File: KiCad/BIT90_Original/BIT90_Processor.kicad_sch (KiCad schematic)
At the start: 24 parts, among them SW65 RST, U1 D4016, U13 74LS138, U14 74LS05, U2 2764, U3 2764, U4 2764, U5 Z80, U6 74LS74, U8 74LS32

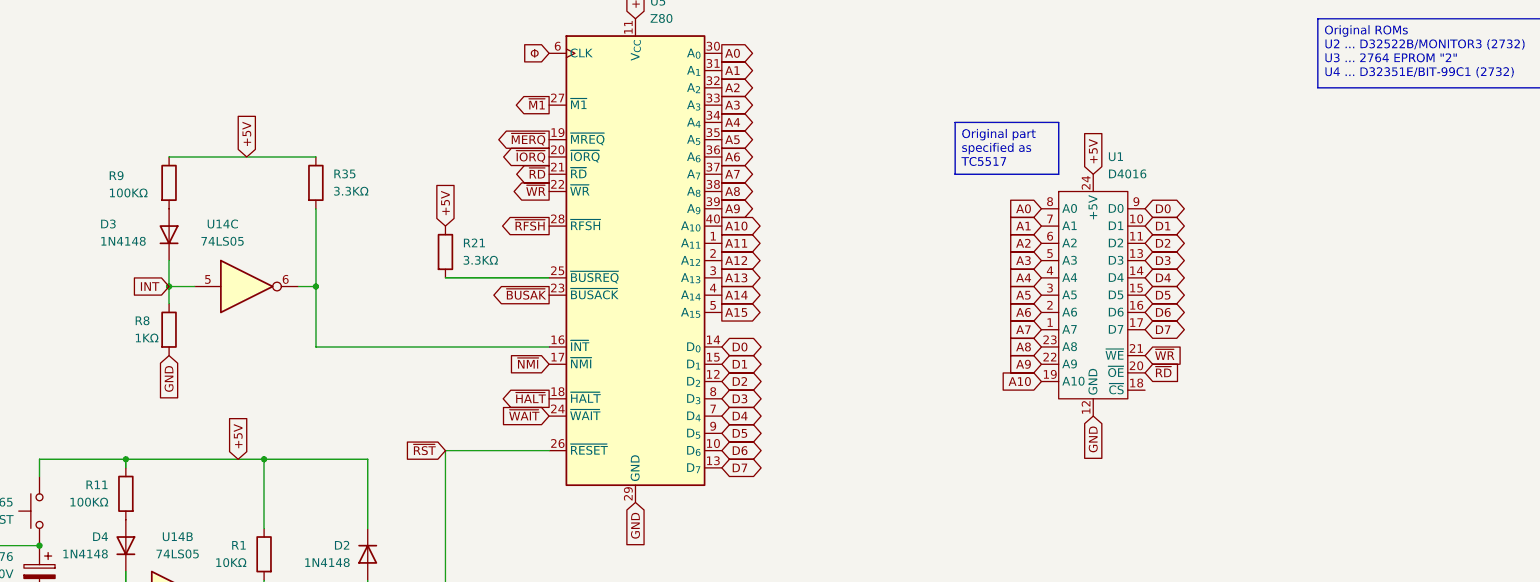
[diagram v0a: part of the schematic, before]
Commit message: Completed keyboard schematic
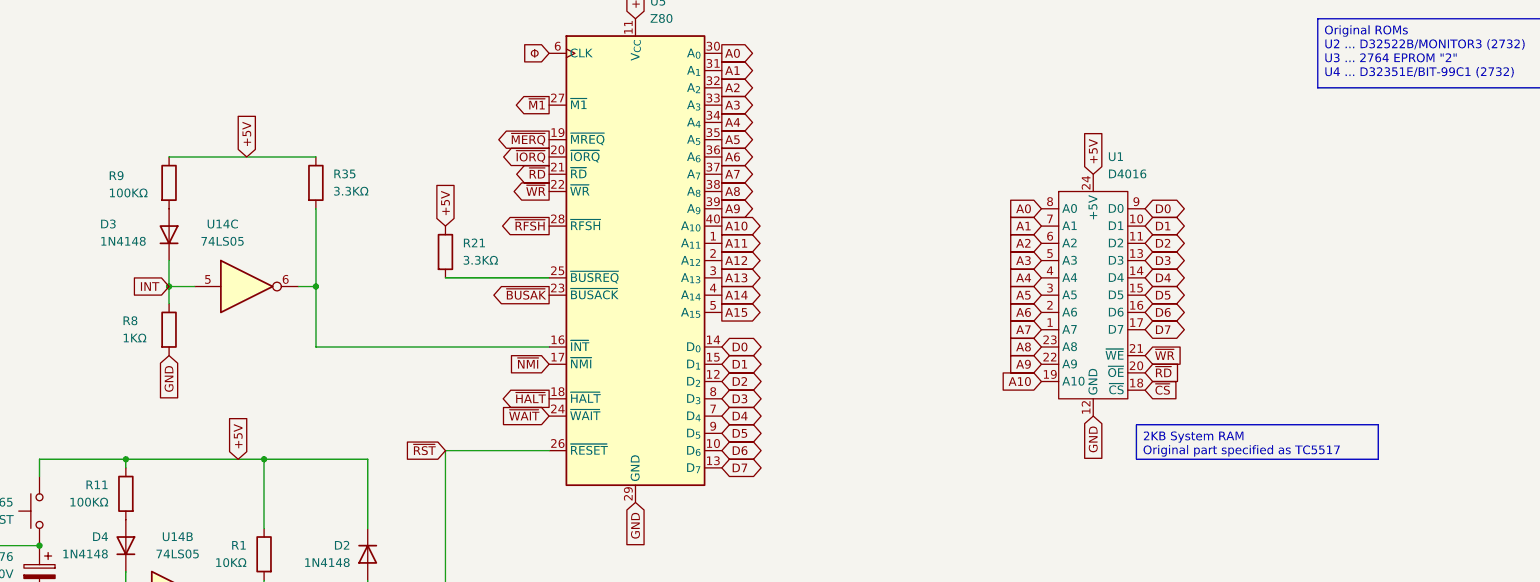
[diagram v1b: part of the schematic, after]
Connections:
- net ~{CS}: now also U1.18 (~{CS})
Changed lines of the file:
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@@
 		(comment 4 "Based on original schematics from BIT Corporation")
 	)
-	(text_box "Original part specified as TC5517"
+	(text_box "2KB System RAM\nOriginal part specified as TC5517"
 		(exclude_from_sim no)
-		(at 176.53 105.41 0)
-		(size 15.24 7.62)
+		(at 203.2 149.86 0)
+		(size 35.56 5.08)
 		(margins 0.9525 0.9525 0.9525 0.9525)
 		(stroke
@@
 		)
 	)
+	(table
+		(column_count 2)
+		(border
+			(external yes)
+			(header yes)
+			(stroke
+				(width 0)
+				(type solid)
+			)
+		)
+		(separators
+			(rows yes)
+			(cols yes)
+			(stroke
+				(width 0)
+				(type solid)
+			)
+		)
+		(column_widths 20.32 20.32)
+		(row_heights 2.54 2.54 2.54 2.54)
+		(cells
+			(table_cell "~{MO}"
+				(exclude_from_sim no)
+				(at 72.39 72.39 0)
+				(size 20.32 2.54)
+				(margins 0.9525 0.9525 0.9525 0.9525)
+				(span 1 1)
+				(fill
+					(type none)
+				)
+				(effects
+					(font
+						(size 1.27 1.27)
+					)
+					(justify left top)
+				)
+			)
+			(table_cell "Monitor"
+				(exclude_from_sim no)
+				(at 92.71 72.39 0)
+				(size 20.32 2.54)
+				(margins 0.9525 0.9525 0.9525 0.9525)
+				(span 1 1)
+				(fill
+					(type none)
+				)
+				(effects
+					(font
+						(size 1.27 1.27)
+					)
+					(justify left top)
+				)
+			)
+			(table_cell "~{BA1} & ~{BA2}"
+				(exclude_from_sim no)
+				(at 72.39 74.93 0)
+				(size 20.32 2.54)
+				(margins 0.9525 0.9525 0.9525 0.9525)
+				(span 1 1)
+				(fill
+					(type none)
+				)
+				(effects
+					(font
+						(size 1.27 1.27)
+					)
+					(justify left top)
+				)
+			)
+			(table_cell "BASIC"
+				(exclude_from_sim no)
+				(at 92.71 74.93 0)
+				(size 20.32 2.54)
+				(margins 0.9525 0.9525 0.9525 0.9525)
+				(span 1 1)
+				(fill
+					(type none)
+				)
+				(effects
+					(font
+						(size 1.27 1.27)
+					)
+					(justify left top)
+				)
+			)
+			(table_cell "~{CS}"
+				(exclude_from_sim no)
+				(at 72.39 77.47 0)
+				(size 20.32 2.54)
+				(margins 0.9525 0.9525 0.9525 0.9525)
+				(span 1 1)
+				(fill
+					(type none)
+				)
+				(effects
+					(font
+						(size 1.27 1.27)
+					)
+					(justify left top)
+				)
+			)
+			(table_cell "System RAM"
+				(exclude_from_sim no)
+				(at 92.71 77.47 0)
+				(size 20.32 2.54)
+				(margins 0.9525 0.9525 0.9525 0.9525)
+				(span 1 1)
+				(fill
+					(type none)
+				)
+				(effects
+					(font
+						(size 1.27 1.27)
+					)
+					(justify left top)
+				)
+			)
+			(table_cell "~{CAR1} to ~{CAR4}"
+				(exclude_from_sim no)
+				(at 72.39 80.01 0)
+				(size 20.32 2.54)
+				(margins 0.9525 0.9525 0.9525 0.9525)
+				(span 1 1)
+				(fill
+					(type none)
+				)
+				(effects
+					(font
+						(size 1.27 1.27)
+					)
+					(justify left top)
+				)
+			)
+			(table_cell "Cartridge"
+				(exclude_from_sim no)
+				(at 92.71 80.01 0)
+				(size 20.32 2.54)
+				(margins 0.9525 0.9525 0.9525 0.9525)
+				(span 1 1)
+				(fill
+					(type none)
+				)
+				(effects
+					(font
+						(size 1.27 1.27)
+					)
+					(justify left top)
+				)
+			)
+		)
+	)
 	(global_label "D4"
 		(shape output)
@@
 		)
 	)
+	(global_label "~{CS}"
+		(shape input)
+		(at 204.47 144.78 0)
+		(fields_autoplaced yes)
+		(effects
+			(font
+				(size 1.27 1.27)
+			)
+			(justify left)
+		)
+		(property "Intersheetrefs" "${INTERSHEET_REFS}"
+			(at 209.9347 144.78 0)
+			(effects
+				(font
+					(size 1.27 1.27)
+				)
+				(justify left)
+				(hide yes)
+			)
+		)
+	)
 	(global_label "A11"
 		(shape input)
@@
 		(dnp no)
 		(property "Reference" "R8"
-			(at 55.88 134.62 0)
+			(at 54.102 134.62 0)
 			(effects
 				(font
@@
 		)
 		(property "Value" "1KΩ"
-			(at 55.88 137.16 0)
+			(at 54.102 137.16 0)
 			(effects
 				(font

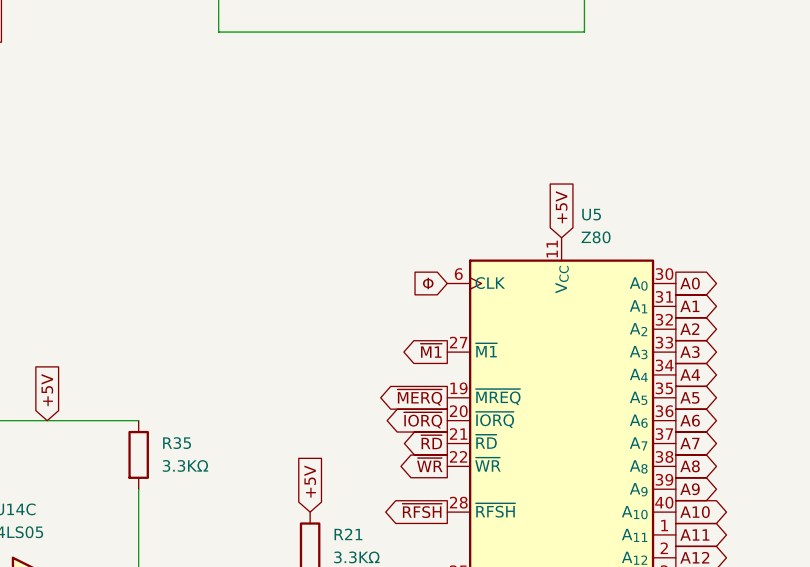
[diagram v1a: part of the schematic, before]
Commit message: Added "Video Control" schematic
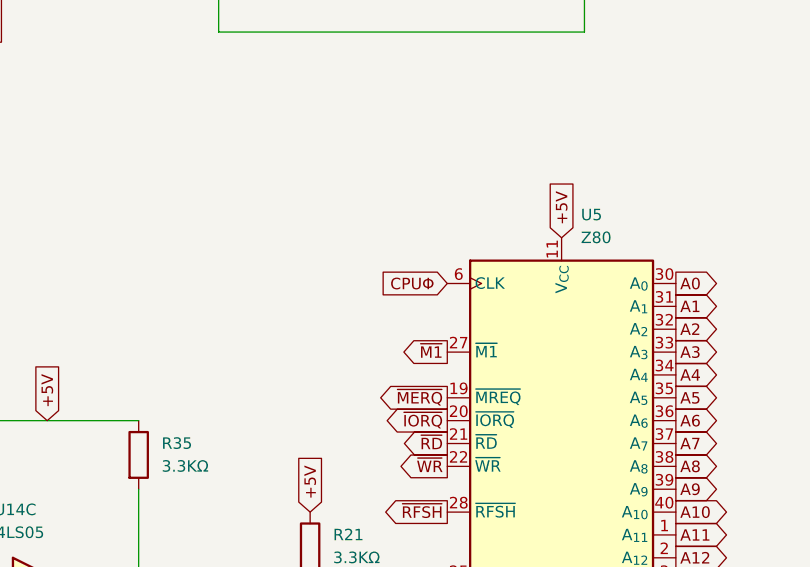
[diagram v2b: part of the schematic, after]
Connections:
- net Φ renamed CPUΦ
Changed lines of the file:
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@@
 		)
 	)
-	(global_label "Φ"
+	(global_label "CPUΦ"
 		(shape input)
 		(at 116.84 95.25 180)
@@
 		)
 		(property "Intersheetrefs" "${INTERSHEET_REFS}"
-			(at 112.5243 95.25 0)
+			(at 108.6538 95.25 0)
 			(effects
 				(font
